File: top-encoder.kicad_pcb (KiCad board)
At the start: 2 copper layers, 8 parts, among them M1 THRU_HOLE_PAD, M2 THRU_HOLE_PAD, M3 THRU_HOLE_PAD, M4 THRU_HOLE_PAD, U2 TLE5009E1000FUMA1

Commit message: designed dogbone
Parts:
- moved C2 22.8 mm to (145.0, 93.8)
- moved M4 21.5 mm to (143.9, 95.2), turned to 180 degrees
- moved C3 19.5 mm to (145.0, 96.7), turned to 90 degrees
- moved M3 18.5 mm to (142.0, 96.8), turned to -90 degrees
- moved U2 17.9 mm to (142.0, 95.2), turned to -90 degrees
- moved M2 17.6 mm to (142.0, 93.8), turned to -90 degrees
- moved M1 14.3 mm to (140.1, 95.2), turned to 180 degrees
- moved C1 11.9 mm to (139.1, 93.7), turned to 90 degrees
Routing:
- net /3v3: track 0.00 -> 4.77 mm
- net /COS: track 0.00 -> 1.40 mm
- net /SIN: track 0.00 -> 1.38 mm
- added copper zone on B.Cu, net GND
- added copper zone on F.Cu, net GND
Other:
- board outline added: 8 x 8 mm

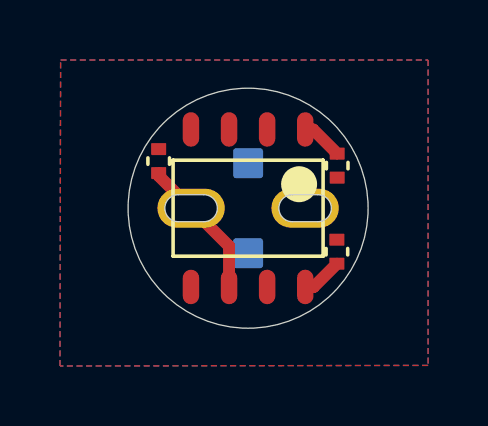
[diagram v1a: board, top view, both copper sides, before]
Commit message: net labelling, silkscreen, boards finished
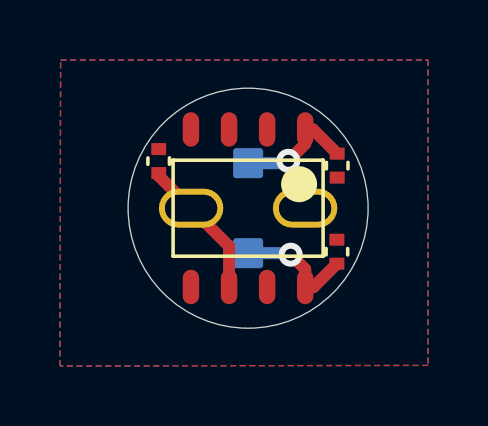
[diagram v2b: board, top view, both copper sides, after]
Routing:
- net /SIN: track 1.38 -> 4.09 mm, vias 0 -> 1
- net /COS: track 1.40 -> 4.05 mm, vias 0 -> 1
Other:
- outline, holes or cut-outs redrawn
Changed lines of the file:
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@@
 (kicad_pcb (version 20221018) (generator pcbnew)
   (general
-    (thickness 1.6)
+    (thickness 1)
   )
   (paper "A4")
@@
   )
   (setup
+    (stackup
+      (layer "F.SilkS" (type "Top Silk Screen"))
+      (layer "F.Paste" (type "Top Solder Paste"))
+      (layer "F.Mask" (type "Top Solder Mask") (thickness 0.01))
+      (layer "F.Cu" (type "copper") (thickness 0.035))
+      (layer "dielectric 1" (type "core") (thickness 0.91) (material "FR4") (epsilon_r 4.5) (loss_tangent 0.02))
+      (layer "B.Cu" (type "copper") (thickness 0.035))
+      (layer "B.Mask" (type "Bottom Solder Mask") (thickness 0.01))
+      (layer "B.Paste" (type "Bottom Solder Paste"))
+      (layer "B.SilkS" (type "Bottom Silk Screen"))
+      (copper_finish "None")
+      (dielectric_constraints no)
+    )
     (pad_to_mask_clearance 0)
     (aux_axis_origin 142.035 95.25)
@@
         (effects (font (size 1 1) (thickness 0.15)))
     )
-    (pad "1" thru_hole oval locked (at 0 0 180) (size 2.25 1.3) (drill oval 1.75 0.9) (layers "*.Cu" "*.Mask")
+    (pad "1" thru_hole oval locked (at 0 0 180) (size 2.15 1.3) (drill oval 1.75 0.9) (layers "*.Cu" "*.Mask")
       (net 1 "GND") (pinfunction "1") (pintype "passive") (thermal_bridge_angle 45))
   )
@@
         (effects (font (size 1 1) (thickness 0.15)))
     )
-    (pad "1" thru_hole oval locked (at 0 0 180) (size 2.25 1.3) (drill oval 1.75 0.9) (layers "*.Cu" "*.Mask")
+    (pad "1" thru_hole oval locked (at 0 0 180) (size 2.15 1.3) (drill oval 1.75 0.9) (layers "*.Cu" "*.Mask")
       (net 4 "/3v3") (pinfunction "1") (pintype "passive") (thermal_bridge_angle 45))
   )
-  (footprint "adapter-encoder:dogbone_pad" (layer "B.Cu")
+  (footprint "adapter-encoder:dogbone_pad" locked (layer "B.Cu")
     (at 142.035 96.75 -90)
     (property "Sheetfile" "top-encoder.kicad_sch")
@@
         (effects (font (size 1 1) (thickness 0.15)) (justify mirror))
     )
-    (pad "1" smd roundrect (at 0 0 270) (size 1 1) (layers "B.Cu" "B.Paste" "B.Mask") (roundrect_rratio 0.1)
+    (pad "1" smd roundrect locked (at 0 0 270) (size 1 1) (layers "B.Cu" "B.Paste" "B.Mask") (roundrect_rratio 0.1)
       (net 3 "/SIN") (pinfunction "1") (pintype "passive") (thermal_bridge_angle 45))
   )
-  (footprint "adapter-encoder:dogbone_pad" (layer "B.Cu")
+  (footprint "adapter-encoder:dogbone_pad" locked (layer "B.Cu")
     (at 142.035 93.75 -90)
     (property "Sheetfile" "top-encoder.kicad_sch")
@@
         (effects (font (size 1 1) (thickness 0.15)) (justify mirror))
     )
-    (pad "1" smd roundrect (at 0 0 270) (size 1 1) (layers "B.Cu" "B.Paste" "B.Mask") (roundrect_rratio 0.1)
+    (pad "1" smd roundrect locked (at 0 0 270) (size 1 1) (layers "B.Cu" "B.Paste" "B.Mask") (roundrect_rratio 0.1)
       (net 2 "/COS") (pinfunction "1") (pintype "passive") (thermal_bridge_angle 45))
   )
-  (gr_line locked (start 143.51 95.7) (end 144.36 95.7)
-    (stroke (width 0.001) (type solid)) (layer "Edge.Cuts"))
-  (gr_arc locked (start 139.71 95.7) (mid 139.26 95.25) (end 139.71 94.8)
-    (stroke (width 0.001) (type solid)) (layer "Edge.Cuts"))
-  (gr_arc locked (start 143.51 95.7) (mid 143.06 95.25) (end 143.51 94.8)
-    (stroke (width 0.001) (type solid)) (layer "Edge.Cuts"))
-  (gr_line locked (start 144.36 94.8) (end 143.51 94.8)
-    (stroke (width 0.001) (type solid)) (layer "Edge.Cuts"))
-  (gr_arc locked (start 144.36 94.8) (mid 144.81 95.25) (end 144.36 95.7)
-    (stroke (width 0.001) (type solid)) (layer "Edge.Cuts"))
   (gr_circle locked (center 142.035 95.25) (end 146.035 95.25)
     (stroke (width 0.001) (type solid)) (fill none) (layer "Edge.Cuts"))
-  (gr_arc locked (start 140.56 94.8) (mid 141.01 95.25) (end 140.56 95.7)
-    (stroke (width 0.001) (type solid)) (layer "Edge.Cuts"))
-  (gr_line locked (start 140.56 94.8) (end 139.71 94.8)
-    (stroke (width 0.001) (type solid)) (layer "Edge.Cuts"))
-  (gr_line locked (start 139.71 95.7) (end 140.56 95.7)
-    (stroke (width 0.001) (type solid)) (layer "Edge.Cuts"))
+  (segment (start 143.94 92.625) (end 143.94 93.105) (width 0.4) (layer "F.Cu") (net 2))
   (segment (start 144.2 92.625) (end 145.005 93.43) (width 0.4) (layer "F.Cu") (net 2))
+  (segment (start 143.94 93.105) (end 143.375 93.67) (width 0.4) (layer "F.Cu") (net 2))
   (segment (start 143.94 92.625) (end 144.2 92.625) (width 0.4) (layer "F.Cu") (net 2))
+  (via (at 143.375 93.67) (size 0.8) (drill 0.4) (layers "F.Cu" "B.Cu") (net 2))
+  (segment (start 142.035 93.75) (end 143.295 93.75) (width 0.4) (layer "B.Cu") (net 2))
+  (segment (start 143.295 93.75) (end 143.375 93.67) (width 0.4) (layer "B.Cu") (net 2))
   (segment (start 144.22 97.875) (end 143.94 97.875) (width 0.4) (layer "F.Cu") (net 3))
+  (segment (start 143.94 97.285) (end 143.455 96.8) (width 0.4) (layer "F.Cu") (net 3))
+  (segment (start 143.94 97.875) (end 143.94 97.285) (width 0.4) (layer "F.Cu") (net 3))
   (segment (start 144.995 97.1) (end 144.22 97.875) (width 0.4) (layer "F.Cu") (net 3))
+  (via (at 143.455 96.8) (size 0.8) (drill 0.4) (layers "F.Cu" "B.Cu") (net 3))
+  (segment (start 142.035 96.75) (end 143.405 96.75) (width 0.4) (layer "B.Cu") (net 3))
+  (segment (start 143.405 96.75) (end 143.455 96.8) (width 0.4) (layer "B.Cu") (net 3))
   (segment (start 139.055 94.08) (end 139.055 94.17) (width 0.4) (layer "F.Cu") (net 4))
   (segment (start 141.4 96.515) (end 140.135 95.25) (width 0.4) (layer "F.Cu") (net 4))
@@
   (group "" locked (id 10ebbebe-dccb-4594-988e-110c02bdaca4)
     (members
-      1142d7f4-f683-4929-9463-aa14f4ac8fc2
-      4d3a78c8-c3a1-474b-a1c9-2d9d31102a74
-      8cbcc632-c788-4854-b8bd-39883684f752
-      9e631cb9-7925-476c-9633-ef6f743f7848
-      a8310b6e-e175-454f-b7e7-707327d15644
       c3d071df-75c7-43a7-beb4-93916a22e4a5
-      d8ffc8a5-d9ff-4c1a-8881-bc6ec2ff2fe2
-      e3e48d0c-83b4-439c-8378-4b86939da332
-      e49b2b9e-a4da-4d0f-b404-0f8808acad56
-    )
-  )
+    )
+  )

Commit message: changed dxf export settings for baseplate. added silk to the encoder portion
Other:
- board text added: "3V3"
- board text added: "COS"
- board text added: "GND"
- board text added: "SIN"
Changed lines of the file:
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@@
   (gr_circle locked (center 142.035 95.25) (end 146.035 95.25)
     (stroke (width 0.001) (type solid)) (fill none) (layer "Edge.Cuts"))
+  (gr_text "3V3" (at 140.105 96.83) (layer "B.SilkS")
+    (effects (font (size 0.5 0.5) (thickness 0.1) bold) (justify left bottom mirror))
+  )
+  (gr_text "COS" (at 142.935 92.9) (layer "B.SilkS")
+    (effects (font (size 0.5 0.5) (thickness 0.1) bold) (justify left bottom mirror))
+  )
+  (gr_text "SIN" (at 142.765 98.4) (layer "B.SilkS")
+    (effects (font (size 0.5 0.5) (thickness 0.1) bold) (justify left bottom mirror))
+  )
+  (gr_text "GND" (at 145.525 96.92) (layer "B.SilkS")
+    (effects (font (size 0.5 0.5) (thickness 0.1) bold) (justify left bottom mirror))
+  )
   (segment (start 143.94 92.625) (end 143.94 93.105) (width 0.4) (layer "F.Cu") (net 2))
   (segment (start 144.2 92.625) (end 145.005 93.43) (width 0.4) (layer "F.Cu") (net 2))
